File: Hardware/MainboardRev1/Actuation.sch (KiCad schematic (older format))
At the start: 28 parts, among them J3 Servo_Control, J4 EMATCH_1: 1586038-2, J5 EMATCH_2: 1586038-2, Q14 SSM3J328R, Q15 NTR4003, Q16 SSM3J328R, Q17 SSM3J328R, Q18 NTR4003, Q19 NTR4003, Q20 SIS612EDNT-T1-GE3, Q21 SIS612EDNT-T1-GE3, U10 LTC4358

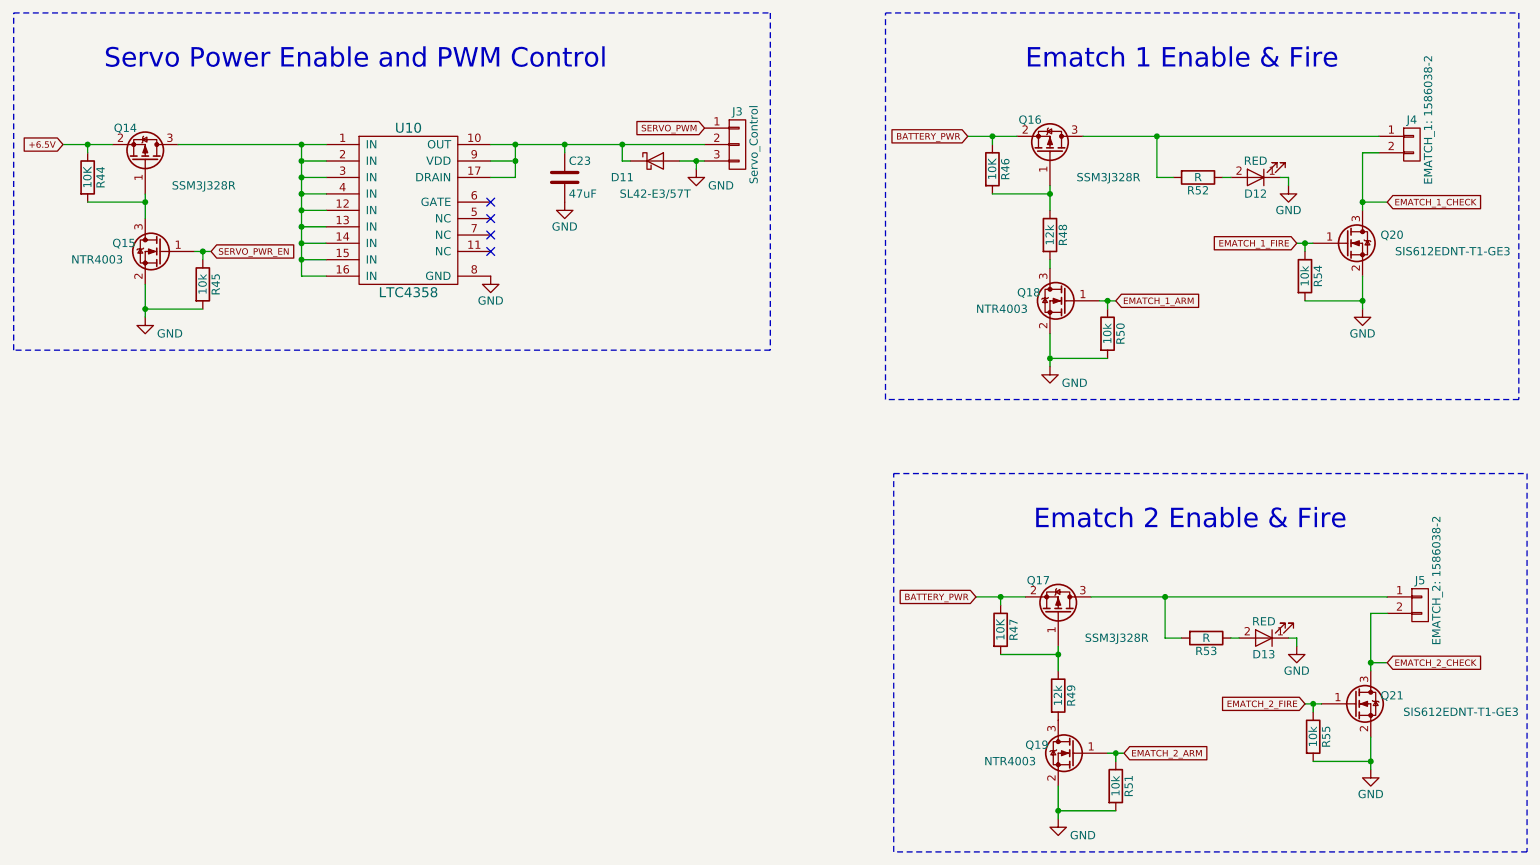
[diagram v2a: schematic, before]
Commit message: Added buzzer and strobe LED. Created BOM. Reannotated. Added sponsors to silkscreen. Needs to be routed and sent out. Good luck Matt!
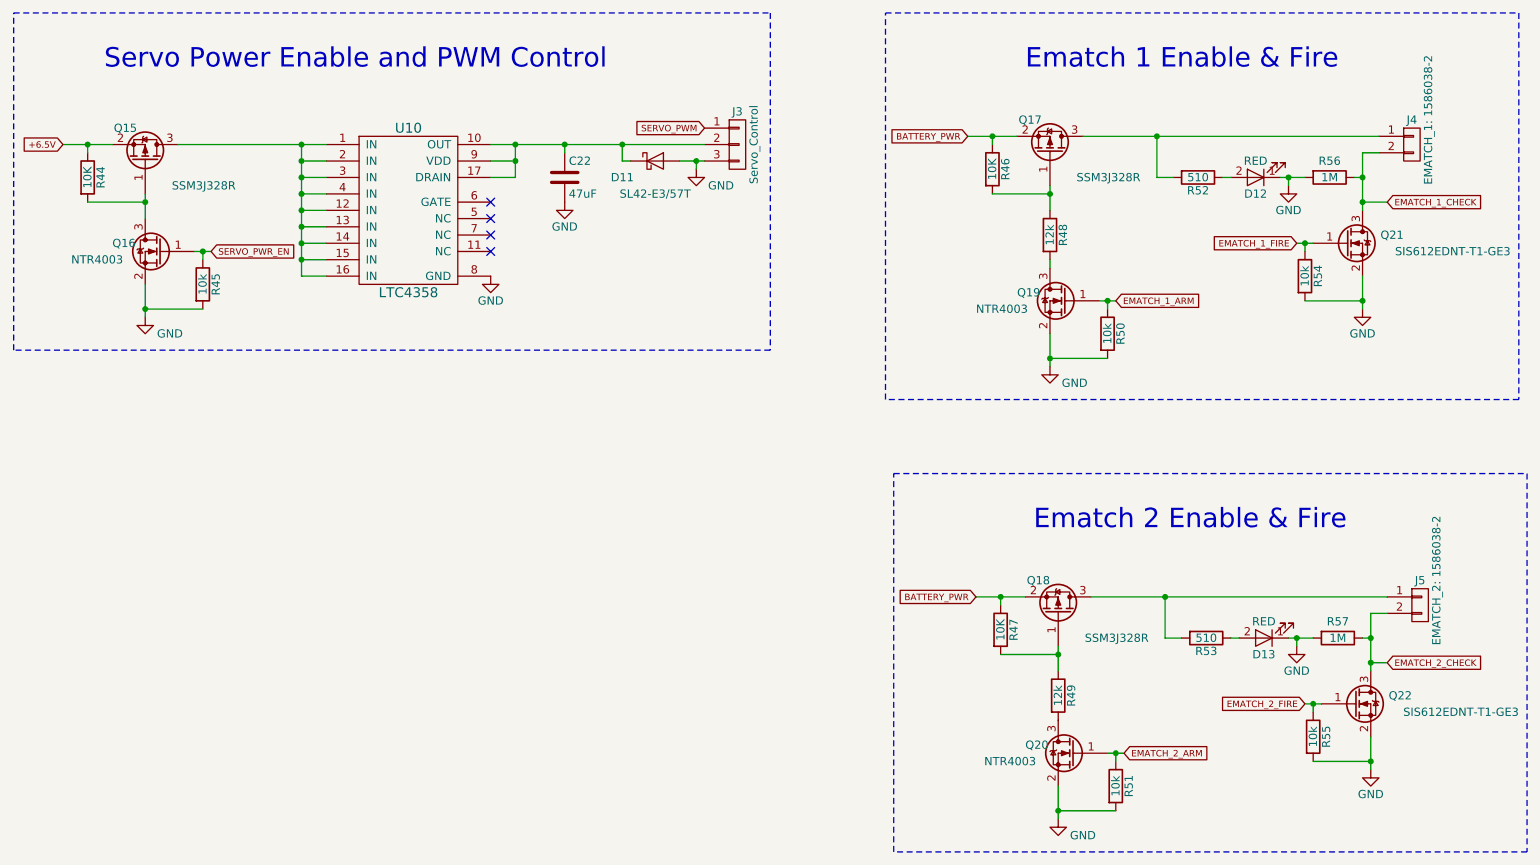
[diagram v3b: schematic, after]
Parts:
- added R56, R57: 1M, Resistors_SMD:R_0603_HandSoldering, symbol R
- R52, R53: value R -> 510
- renumbered C23 to C22, Q14 to Q15, Q15 to Q16, Q16 to Q17, Q17 to Q18, Q18 to Q19, Q19 to Q20, Q20 to Q21, Q21 to Q22
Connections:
- net EMATCH_1_CHECK: now also R56.1
- net EMATCH_2_CHECK: now also R57.1
- net GND: now also R56.2, R57.2
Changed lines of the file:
@@
 +6.5V
 $Comp
-L GND #PWR042
+L GND #PWR040
 U 1 1 5AF9BFAC
 P 3900 2650
-F 0 "#PWR042" H 3900 2400 50  0001 C CNN
+F 0 "#PWR040" H 3900 2400 50  0001 C CNN
 F 1 "GND" H 3900 2500 50  0000 C CNN
 F 2 "" H 3900 2650 50  0000 C CNN
@@
 NoConn ~ 3900 2200
 $Comp
-L Q_PMOS_GSD Q14
+L Q_PMOS_GSD Q15
 U 1 1 5AF9DC31
 P 1800 1950
-F 0 "Q14" V 2000 1900 50  0000 R CNN
+F 0 "Q15" V 2000 1900 50  0000 R CNN
 F 1 "SSM3J328R" V 1650 2500 50  0000 R CNN
 F 2 "TO_SOT_Packages_SMD:SOT-23" H 2000 2050 50  0001 C CNN
@@
 $EndComp
 $Comp
-L GND #PWR043
+L GND #PWR041
 U 1 1 5AF9DC38
 P 1800 2900
-F 0 "#PWR043" H 1800 2650 50  0001 C CNN
+F 0 "#PWR041" H 1800 2650 50  0001 C CNN
 F 1 "GND" H 1950 2800 50  0000 C CNN
 F 2 "" H 1800 2900 50  0000 C CNN
@@
 $EndComp
 $Comp
-L Q_NMOS_GSD Q15
+L Q_NMOS_GSD Q16
 U 1 1 5AF9DC4D
 P 1900 2500
-F 0 "Q15" H 2200 2550 50  0000 R CNN
+F 0 "Q16" H 2200 2550 50  0000 R CNN
 F 1 "NTR4003" H 2450 2450 50  0000 R CNN
 F 2 "TO_SOT_Packages_SMD:SOT-23" H 2100 2600 50  0001 C CNN
@@
 SERVO_PWR_EN
 $Comp
-L C C23
+L C C22
 U 1 1 5AF9DFB4
 P 4350 2050
-F 0 "C23" H 4375 2150 50  0000 L CNN
+F 0 "C22" H 4375 2150 50  0000 L CNN
 F 1 "47uF" H 4375 1950 50  0000 L CNN
 F 2 "Capacitors_SMD:C_1210_HandSoldering" H 4388 1900 50  0001 C CNN
@@
 $EndComp
 $Comp
-L GND #PWR044
+L GND #PWR042
 U 1 1 5AF9E058
 P 4350 2200
-F 0 "#PWR044" H 4350 1950 50  0001 C CNN
+F 0 "#PWR042" H 4350 1950 50  0001 C CNN
 F 1 "GND" H 4350 2050 50  0000 C CNN
 F 2 "" H 4350 2200 50  0000 C CNN
@@
 $EndComp
 $Comp
-L GND #PWR045
+L GND #PWR043
 U 1 1 5AF9E824
 P 5150 2000
-F 0 "#PWR045" H 5150 1750 50  0001 C CNN
+F 0 "#PWR043" H 5150 1750 50  0001 C CNN
 F 1 "GND" H 5300 1900 50  0000 C CNN
 F 2 "" H 5150 2000 50  0000 C CNN
@@
 	1000 3100 1000 1050
 $Comp
-L Q_PMOS_GSD Q16
+L Q_PMOS_GSD Q17
 U 1 1 5AFA6867
 P 7300 1900
-F 0 "Q16" V 7500 1850 50  0000 R CNN
+F 0 "Q17" V 7500 1850 50  0000 R CNN
 F 1 "SSM3J328R" V 7150 2450 50  0000 R CNN
 F 2 "TO_SOT_Packages_SMD:SOT-23" H 7500 2000 50  0001 C CNN
@@
 $EndComp
 $Comp
-L GND #PWR046
+L GND #PWR044
 U 1 1 5AFA686D
 P 7300 3200
-F 0 "#PWR046" H 7300 2950 50  0001 C CNN
+F 0 "#PWR044" H 7300 2950 50  0001 C CNN
 F 1 "GND" H 7450 3100 50  0000 C CNN
 F 2 "" H 7300 3200 50  0000 C CNN
@@
 $EndComp
 $Comp
-L Q_NMOS_GSD Q18
+L Q_NMOS_GSD Q19
 U 1 1 5AFA687F
 P 7400 2800
-F 0 "Q18" H 7700 2850 50  0000 R CNN
+F 0 "Q19" H 7700 2850 50  0000 R CNN
 F 1 "NTR4003" H 7950 2750 50  0000 R CNN
 F 2 "TO_SOT_Packages_SMD:SOT-23" H 7600 2900 50  0001 C CNN
@@
 $EndComp
 $Comp
-L Q_NMOS_GSD Q20
+L Q_NMOS_GSD Q21
 U 1 1 5AFA7B1B
 P 9100 2450
-F 0 "Q20" H 9450 2500 50  0000 R CNN
+F 0 "Q21" H 9450 2500 50  0000 R CNN
 F 1 "SIS612EDNT-T1-GE3" H 10100 2400 50  0000 R CNN
 F 2 "Dans_Parts:PowerPAK_1212-8S" H 9300 2550 50  0001 C CNN
@@
 	9200 2650 9200 2850
 $Comp
-L GND #PWR047
+L GND #PWR045
 U 1 1 5AFA7F4E
 P 9200 2850
-F 0 "#PWR047" H 9200 2600 50  0001 C CNN
+F 0 "#PWR045" H 9200 2600 50  0001 C CNN
 F 1 "GND" H 9200 2700 50  0000 C CNN
 F 2 "" H 9200 2850 50  0000 C CNN
@@
 $EndComp
 $Comp
-L GND #PWR048
+L GND #PWR046
 U 1 1 5AFAA805
 P 8750 2100
-F 0 "#PWR048" H 8750 1850 50  0001 C CNN
+F 0 "#PWR046" H 8750 1850 50  0001 C CNN
 F 1 "GND" H 8750 1950 50  0000 C CNN
 F 2 "" H 8750 2100 50  0000 C CNN
@@
 	8750 2100 8750 2050
 Wire Wire Line
-	8750 2050 8700 2050
+	8700 2050 8850 2050
 $Comp
 L R R52
@@
 P 8200 2050
 F 0 "R52" V 8280 2050 50  0000 C CNN
-F 1 "R" V 8200 2050 50  0000 C CNN
+F 1 "510" V 8200 2050 50  0000 C CNN
 F 2 "Resistors_SMD:R_0603_HandSoldering" V 8130 2050 50  0001 C CNN
 F 3 "" H 8200 2050 50  0000 C CNN
@@
 	6300 3400 6300 1050
 $Comp
-L Q_PMOS_GSD Q17
+L Q_PMOS_GSD Q18
 U 1 1 5AFAB31C
 P 7350 4700
-F 0 "Q17" V 7550 4650 50  0000 R CNN
+F 0 "Q18" V 7550 4650 50  0000 R CNN
 F 1 "SSM3J328R" V 7200 5250 50  0000 R CNN
 F 2 "TO_SOT_Packages_SMD:SOT-23" H 7550 4800 50  0001 C CNN
@@
 $EndComp
 $Comp
-L GND #PWR049
+L GND #PWR047
 U 1 1 5AFAB322
 P 7350 5950
-F 0 "#PWR049" H 7350 5700 50  0001 C CNN
+F 0 "#PWR047" H 7350 5700 50  0001 C CNN
 F 1 "GND" H 7500 5850 50  0000 C CNN
 F 2 "" H 7350 5950 50  0000 C CNN
@@
 $EndComp
 $Comp
-L Q_NMOS_GSD Q19
+L Q_NMOS_GSD Q20
 U 1 1 5AFAB334
 P 7450 5550
-F 0 "Q19" H 7750 5600 50  0000 R CNN
+F 0 "Q20" H 7750 5600 50  0000 R CNN
 F 1 "NTR4003" H 8000 5500 50  0000 R CNN
 F 2 "TO_SOT_Packages_SMD:SOT-23" H 7650 5650 50  0001 C CNN
@@
 $EndComp
 $Comp
-L Q_NMOS_GSD Q21
+L Q_NMOS_GSD Q22
 U 1 1 5AFAB34E
 P 9150 5250
-F 0 "Q21" H 9450 5300 50  0000 R CNN
+F 0 "Q22" H 9500 5300 50  0000 R CNN
 F 1 "SIS612EDNT-T1-GE3" H 10150 5200 50  0000 R CNN
 F 2 "Dans_Parts:PowerPAK_1212-8S" H 9350 5350 50  0001 C CNN
@@
 	9250 5450 9250 5650
 $Comp
-L GND #PWR050
+L GND #PWR048
 U 1 1 5AFAB35E
 P 9250 5650
-F 0 "#PWR050" H 9250 5400 50  0001 C CNN
+F 0 "#PWR048" H 9250 5400 50  0001 C CNN
 F 1 "GND" H 9250 5500 50  0000 C CNN
 F 2 "" H 9250 5650 50  0000 C CNN
@@
 $EndComp
 $Comp
-L GND #PWR051
+L GND #PWR049
 U 1 1 5AFAB370
 P 8800 4900
-F 0 "#PWR051" H 8800 4650 50  0001 C CNN
+F 0 "#PWR049" H 8800 4650 50  0001 C CNN
 F 1 "GND" H 8800 4750 50  0000 C CNN
 F 2 "" H 8800 4900 50  0000 C CNN
@@
 	8800 4900 8800 4850
 Wire Wire Line
-	8800 4850 8750 4850
+	8750 4850 8900 4850
 $Comp
 L R R53
@@
 P 8250 4850
 F 0 "R53" V 8330 4850 50  0000 C CNN
-F 1 "R" V 8250 4850 50  0000 C CNN
+F 1 "510" V 8250 4850 50  0000 C CNN
 F 2 "Resistors_SMD:R_0603_HandSoldering" V 8180 4850 50  0001 C CNN
 F 3 "" H 8250 4850 50  0000 C CNN
@@
 Connection ~ 2750 2550
 NoConn ~ 3900 2500
+$Comp
+L R R56
+U 1 1 5B04179E
+P 9000 2050
+F 0 "R56" V 8900 2050 50  0000 C CNN
+F 1 "1M" V 9000 2050 50  0000 C CNN
+F 2 "Resistors_SMD:R_0603_HandSoldering" V 8930 2050 50  0001 C CNN
+F 3 "" H 9000 2050 50  0001 C CNN
+	1    9000 2050
+	0    1    1    0
+$EndComp
+Connection ~ 8750 2050
+Wire Wire Line
+	9150 2050 9200 2050
+Connection ~ 9200 2050
+$Comp
+L R R57
+U 1 1 5B041DFE
+P 9050 4850
+F 0 "R57" V 8950 4850 50  0000 C CNN
+F 1 "1M" V 9050 4850 50  0000 C CNN
+F 2 "Resistors_SMD:R_0603_HandSoldering" V 8980 4850 50  0001 C CNN
+F 3 "" H 9050 4850 50  0001 C CNN
+	1    9050 4850
+	0    1    1    0
+$EndComp
+Connection ~ 8800 4850
+Wire Wire Line
+	9200 4850 9250 4850
+Connection ~ 9250 4850
 $EndSCHEMATC
